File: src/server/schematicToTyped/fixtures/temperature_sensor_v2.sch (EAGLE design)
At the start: 1 part, among them U1 MCP9808

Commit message: Cleaning json output format
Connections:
- net [('TYPE','I2C'),('NUMBER',0),('SIGNAL','SDA'),('VOLTAGE',3.3)] renamed [('TYPE','I2C'),('NUMBER',0),('SIGNAL','SDA'),('VOLTAGE_RANGE','[3.3,4]')]
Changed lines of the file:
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@@
 </segment>
 </net>
-<net name="[('TYPE','I2C'),('NUMBER',0),('SIGNAL','SDA'),('VOLTAGE',3.3)]" class="0">
+<net name="[('TYPE','I2C'),('NUMBER',0),('SIGNAL','SDA'),('VOLTAGE_RANGE','[3.3,4]')]" class="0">
 <segment>
 <pinref part="U1" gate="G$1" pin="SDA"/>

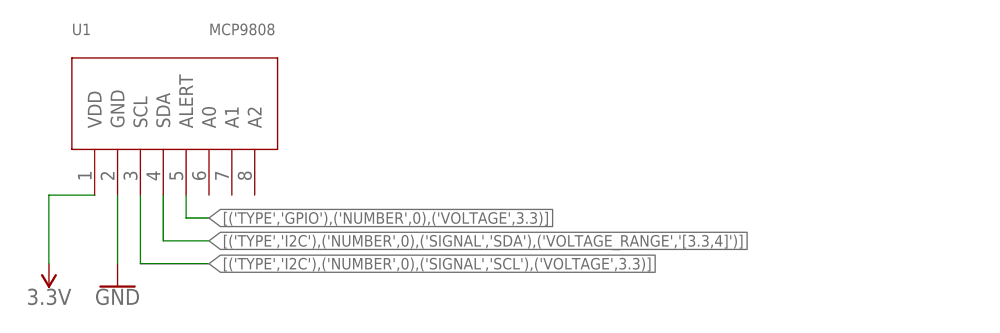
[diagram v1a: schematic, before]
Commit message: Improving typed schematics
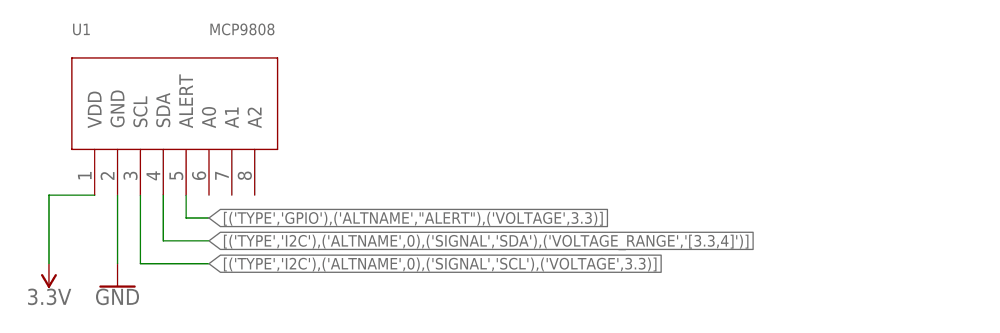
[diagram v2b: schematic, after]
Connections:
- net [('TYPE','GPIO'),('NUMBER',0),('VOLTAGE',3.3)] renamed [('TYPE','GPIO'),('ALTNAME',"ALERT"),('VOLTAGE',3.3)]
- net [('TYPE','I2C'),('NUMBER',0),('SIGNAL','SCL'),('VOLTAGE',3.3)] renamed [('TYPE','I2C'),('ALTNAME',0),('SIGNAL','SCL'),('VOLTAGE',3.3)]
- net [('TYPE','I2C'),('NUMBER',0),('SIGNAL','SDA'),('VOLTAGE_RANGE','[3.3,4]')] renamed [('TYPE','I2C'),('ALTNAME',0),('SIGNAL','SDA'),('VOLTAGE_RANGE','[3.3,4]')]
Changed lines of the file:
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@@
 </segment>
 </net>
-<net name="[('TYPE','I2C'),('NUMBER',0),('SIGNAL','SCL'),('VOLTAGE',3.3)]" class="0">
+<net name="[('TYPE','I2C'),('ALTNAME',0),('SIGNAL','SCL'),('VOLTAGE',3.3)]" class="0">
 <segment>
 <pinref part="U1" gate="G$1" pin="SCL"/>
@@
 </segment>
 </net>
-<net name="[('TYPE','I2C'),('NUMBER',0),('SIGNAL','SDA'),('VOLTAGE_RANGE','[3.3,4]')]" class="0">
+<net name="[('TYPE','I2C'),('ALTNAME',0),('SIGNAL','SDA'),('VOLTAGE_RANGE','[3.3,4]')]" class="0">
 <segment>
 <pinref part="U1" gate="G$1" pin="SDA"/>
@@
 </segment>
 </net>
-<net name="[('TYPE','GPIO'),('NUMBER',0),('VOLTAGE',3.3)]" class="0">
+<net name="[('TYPE','GPIO'),('ALTNAME',&quot;ALERT&quot;),('VOLTAGE',3.3)]" class="0">
 <segment>
 <pinref part="U1" gate="G$1" pin="ALERT"/>
